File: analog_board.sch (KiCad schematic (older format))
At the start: 53 parts, among them J301 SAMTEC-TSW-105-07-X-D, J302 SAMTEC-TSW-105-07-X-D, J304 SAMTEC-TSW-105-07-X-D, J305 SAMTEC-TSW-105-07-X-D, U1 LM324, U3 AD620, U4 AD620

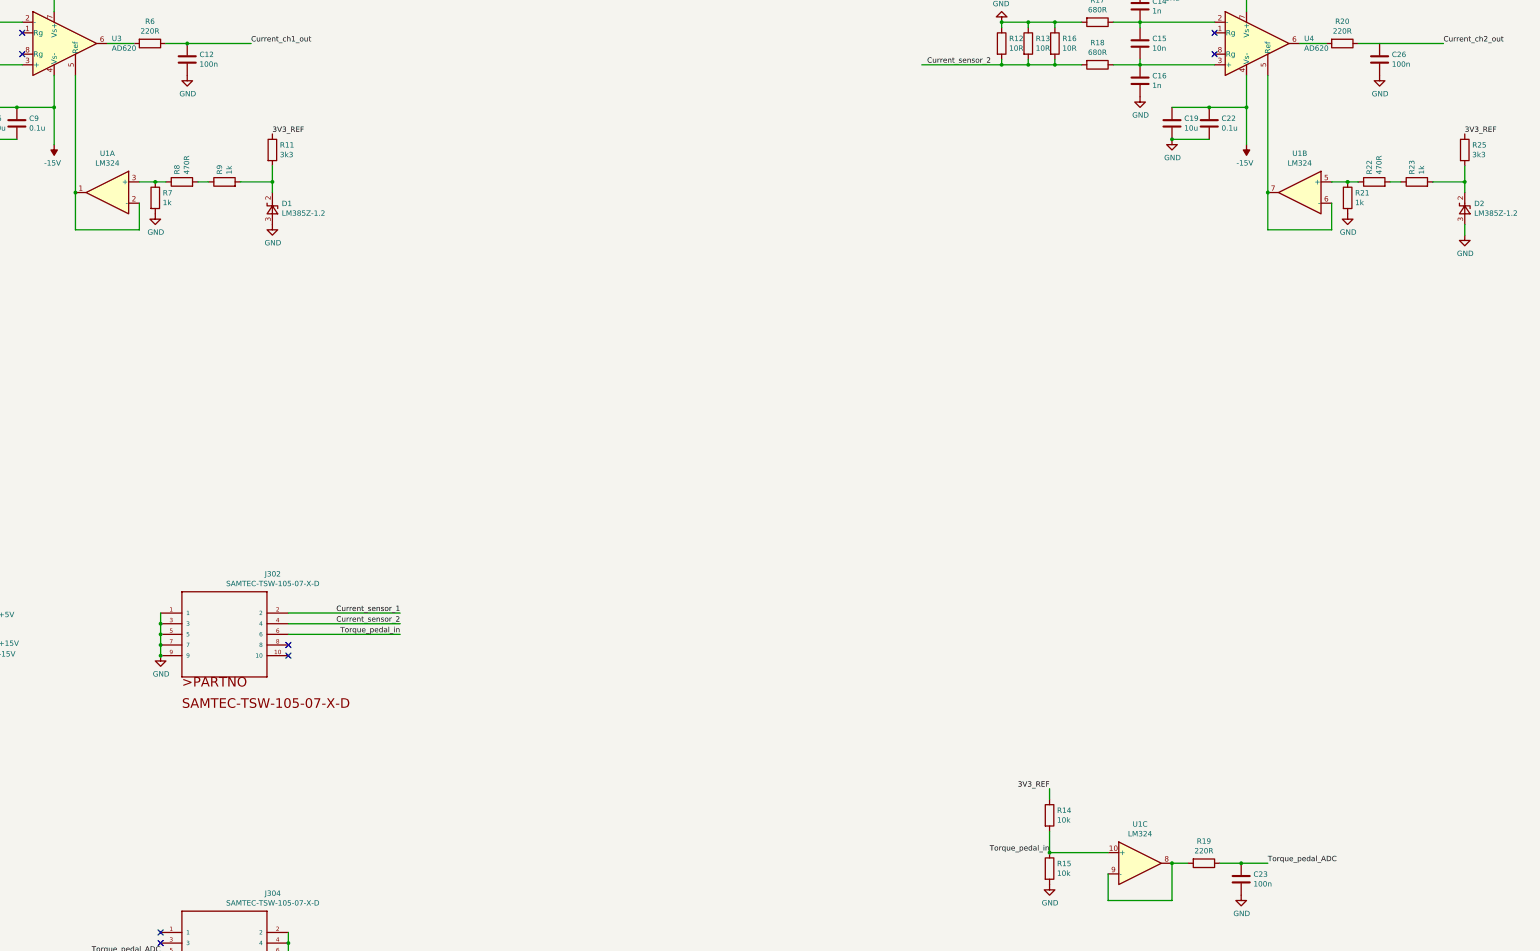
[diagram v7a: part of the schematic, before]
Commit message: Removed te reference amp of current_ch2, layed out components No wiring yet.
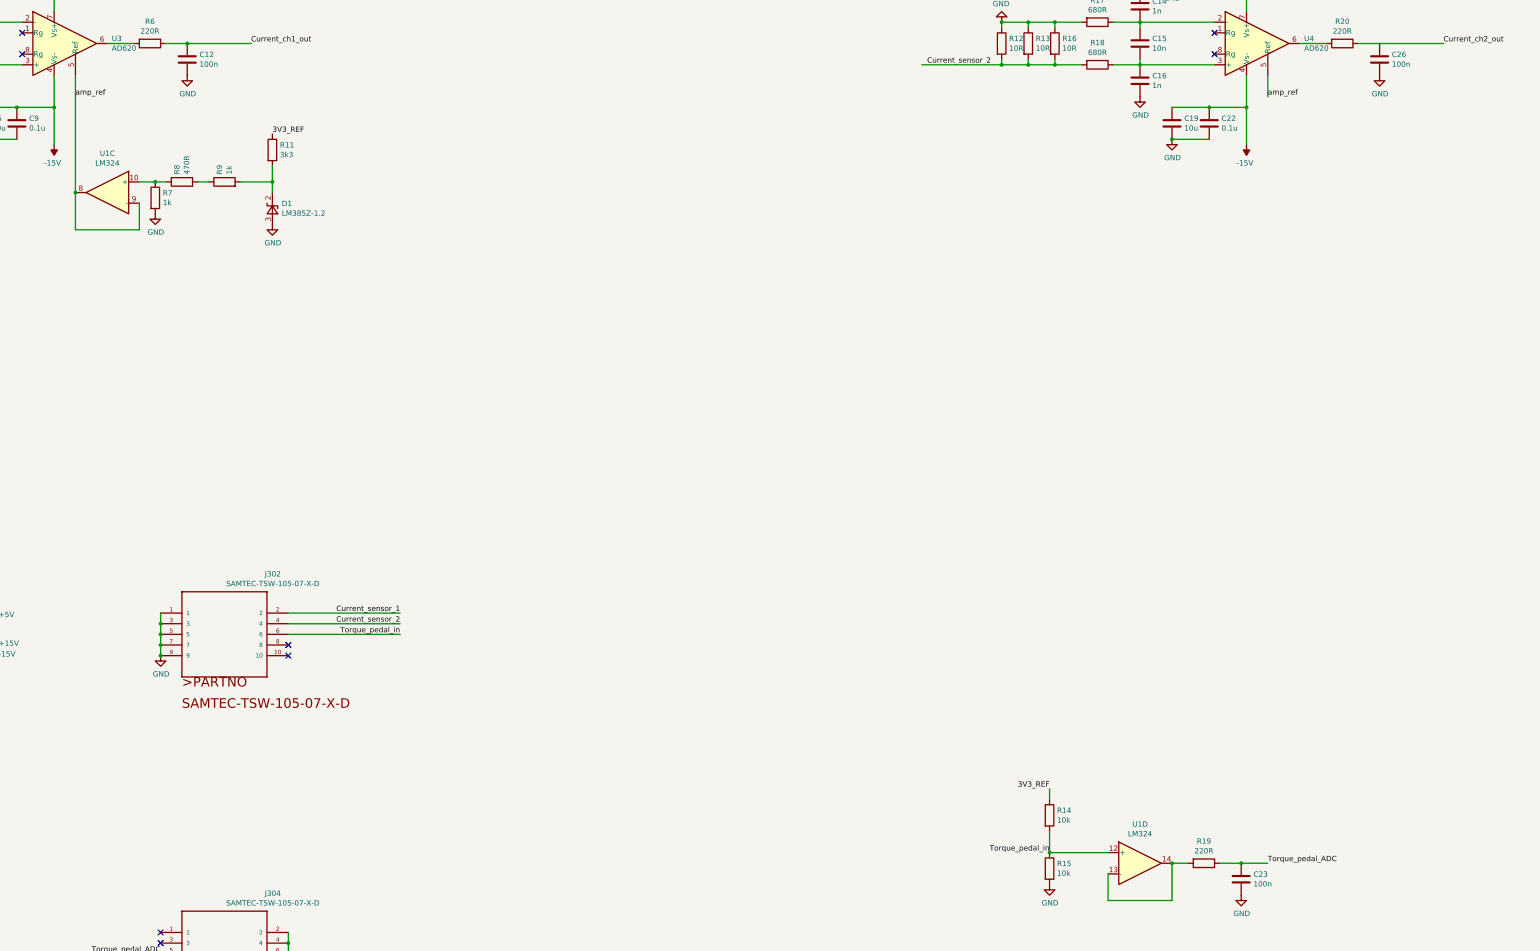
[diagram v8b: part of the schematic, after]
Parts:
- removed D2: LM385Z-1.2, Package_TO_SOT_THT:TO-92_Inline, symbol Reference_Voltage:LM385Z-1.2
- removed R21, R23: 1k, Resistor_SMD:R_0805_2012Metric_Pad1.15x1.40mm_HandSolder, symbol Device:R
- removed R22: 470R, Resistor_SMD:R_0805_2012Metric_Pad1.15x1.40mm_HandSolder, symbol Device:R
- removed R25: 3k3, Resistor_SMD:R_0805_2012Metric_Pad1.15x1.40mm_HandSolder, symbol Device:R
- removed unit 2 of U1
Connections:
- net Torque_pedal_in: now also U1.12 (+); no longer U1.10 (+)
- net at R7.1, R8.1: now also U1.10 (+); no longer U1.3 (+)
- net amp_ref: now reaches U4.5 (Ref)
- net amp_ref: now also U1.8, U1.9 (-), U3.5 (Ref)
- new net: R19.2, U1.13 (-), U1.14
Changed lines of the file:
@@
 $Comp
 L Amplifier_Operational:LM324 U1
-U 1 1 5C6FEAFE
+U 3 1 5C6FEAFE
 P 4950 6000
 F 0 "U1" H 4950 6367 50  0000 C CNN
@@
 F 2 "Package_DIP:DIP-14_W7.62mm" H 4900 6100 50  0001 C CNN
 F 3 "http://www.ti.com/lit/ds/symlink/lm2902-n.pdf" H 5000 6200 50  0001 C CNN
-	1    4950 6000
+	3    4950 6000
 	-1   0    0    -1
 $EndComp
@@
 Text Label 12650 4800 0    50   ~ 0
 Current_sensor_2
-Wire Wire Line
-	16450 6100 16450 6350
 Text Label 17500 4600 0    50   ~ 0
 Current_ch2_out
@@
 $Comp
 L Amplifier_Operational:LM324 U1
-U 3 1 5C73D7CC
+U 4 1 5C73D7CC
 P 14650 12300
 F 0 "U1" H 14650 12667 50  0000 C CNN
@@
 F 2 "Package_DIP:DIP-14_W7.62mm" H 14600 12400 50  0001 C CNN
 F 3 "http://www.ti.com/lit/ds/symlink/lm2902-n.pdf" H 14700 12500 50  0001 C CNN
-	3    14650 12300
+	4    14650 12300
 	1    0    0    -1
 $EndComp
@@
 Wire Wire Line
 	13800 11700 13800 11600
-$Comp
-L Amplifier_Operational:LM324 U1
-U 2 1 5C78DB94
-P 16150 6000
-F 0 "U1" H 16150 6367 50  0000 C CNN
-F 1 "LM324" H 16150 6276 50  0000 C CNN
-F 2 "Package_DIP:DIP-14_W7.62mm" H 16100 6100 50  0001 C CNN
-F 3 "http://www.ti.com/lit/ds/symlink/lm2902-n.pdf" H 16200 6200 50  0001 C CNN
-	2    16150 6000
-	-1   0    0    -1
-$EndComp
 Text Label 13800 12200 2    50   ~ 0
 Torque_pedal_in
@@
 	4650 6350 5250 6350
 Connection ~ 4650 6000
-Wire Wire Line
-	15850 6000 15850 6350
-Wire Wire Line
-	15850 6350 16450 6350
-Connection ~ 15850 6000
 $Comp
 L Device:R R6
@@
 Wire Wire Line
 	4650 4900 4650 6000
-Wire Wire Line
-	15850 4900 15850 6000
 Connection ~ 3650 1650
 $Comp
@@
 	1    0    0    -1
 $EndComp
-$Comp
-L Reference_Voltage:LM385Z-1.2 D2
-U 1 1 5C873D8A
-P 17700 6150
-F 0 "D2" V 17746 6062 50  0000 R CNN
-F 1 "LM385Z-1.2" V 17655 6062 50  0000 R CNN
-F 2 "Package_TO_SOT_THT:TO-92_Inline" H 17700 5950 50  0001 C CIN
-F 3 "http://www.onsemi.com/pub_link/Collateral/LM285-D.PDF" H 17700 6150 50  0001 C CIN
-	1    17700 6150
-	0    -1   -1   0
-$EndComp
-$Comp
-L power:GND #PWR0138
-U 1 1 5C873D91
-P 17700 6400
-F 0 "#PWR0138" H 17700 6150 50  0001 C CNN
-F 1 "GND" H 17705 6227 50  0000 C CNN
-F 2 "" H 17700 6400 50  0001 C CNN
-F 3 "" H 17700 6400 50  0001 C CNN
-	1    17700 6400
-	1    0    0    -1
-$EndComp
-$Comp
-L Device:R R25
-U 1 1 5C873D97
-P 17700 5600
-F 0 "R25" H 17770 5646 50  0000 L CNN
-F 1 "3k3" H 17770 5555 50  0000 L CNN
-F 2 "Resistor_SMD:R_0805_2012Metric_Pad1.15x1.40mm_HandSolder" V 17630 5600 50  0001 C CNN
-F 3 "~" H 17700 5600 50  0001 C CNN
-	1    17700 5600
-	1    0    0    -1
-$EndComp
-Text Label 17700 5450 0    50   ~ 0
-3V3_REF
-$Comp
-L Device:R R21
-U 1 1 5C873DAB
-P 16600 6050
-F 0 "R21" H 16670 6096 50  0000 L CNN
-F 1 "1k" H 16670 6005 50  0000 L CNN
-F 2 "Resistor_SMD:R_0805_2012Metric_Pad1.15x1.40mm_HandSolder" V 16530 6050 50  0001 C CNN
-F 3 "~" H 16600 6050 50  0001 C CNN
-	1    16600 6050
-	1    0    0    -1
-$EndComp
-$Comp
-L Device:R R23
-U 1 1 5C873DB2
-P 17250 5900
-F 0 "R23" H 17320 5946 50  0000 L CNN
-F 1 "1k" H 17320 5855 50  0000 L CNN
-F 2 "Resistor_SMD:R_0805_2012Metric_Pad1.15x1.40mm_HandSolder" V 17180 5900 50  0001 C CNN
-F 3 "~" H 17250 5900 50  0001 C CNN
-	1    17250 5900
-	0    -1   -1   0
-$EndComp
-$Comp
-L Device:R R22
-U 1 1 5C873DB9
-P 16850 5900
-F 0 "R22" H 16920 5946 50  0000 L CNN
-F 1 "470R" H 16920 5855 50  0000 L CNN
-F 2 "Resistor_SMD:R_0805_2012Metric_Pad1.15x1.40mm_HandSolder" V 16780 5900 50  0001 C CNN
-F 3 "~" H 16850 5900 50  0001 C CNN
-	1    16850 5900
-	0    -1   -1   0
-$EndComp
-Wire Wire Line
-	17100 5900 17000 5900
-Wire Wire Line
-	16450 5900 16600 5900
-Wire Wire Line
-	16600 5900 16700 5900
-Connection ~ 16600 5900
-$Comp
-L power:GND #PWR0139
-U 1 1 5C873DC6
-P 16600 6200
-F 0 "#PWR0139" H 16600 5950 50  0001 C CNN
-F 1 "GND" H 16605 6027 50  0000 C CNN
-F 2 "" H 16600 6200 50  0001 C CNN
-F 3 "" H 16600 6200 50  0001 C CNN
-	1    16600 6200
-	1    0    0    -1
-$EndComp
 Wire Wire Line
 	6500 6000 6500 5900
@@
 	6500 5900 6500 5750
 Connection ~ 6500 5900
-Wire Wire Line
-	17400 5900 17700 5900
-Wire Wire Line
-	17700 5900 17700 5750
-Wire Wire Line
-	17700 6000 17700 5900
-Connection ~ 17700 5900
 Wire Wire Line
 	6200 5900 6500 5900
@@
 NoConn ~ 1550 13250
 NoConn ~ 1550 13350
-Wire Wire Line
-	17700 6400 17700 6300
 Connection ~ 5700 4600
 Wire Wire Line
 	17500 4600 16900 4600
 NoConn ~ 2750 10050
+Text Label 4650 5100 0    50   ~ 0
+amp_ref
+Text Label 15850 5100 0    50   ~ 0
+amp_ref
+Wire Wire Line
+	15850 4900 15850 5100
 $EndSCHEMATC
